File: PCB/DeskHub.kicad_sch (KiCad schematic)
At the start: 73 parts, among them J1 USB_A, J2 5V Barrel, U1 TUSB4041I, U3 Dual Voltage Regulator, Y1 ECS-240-20-30B-TR

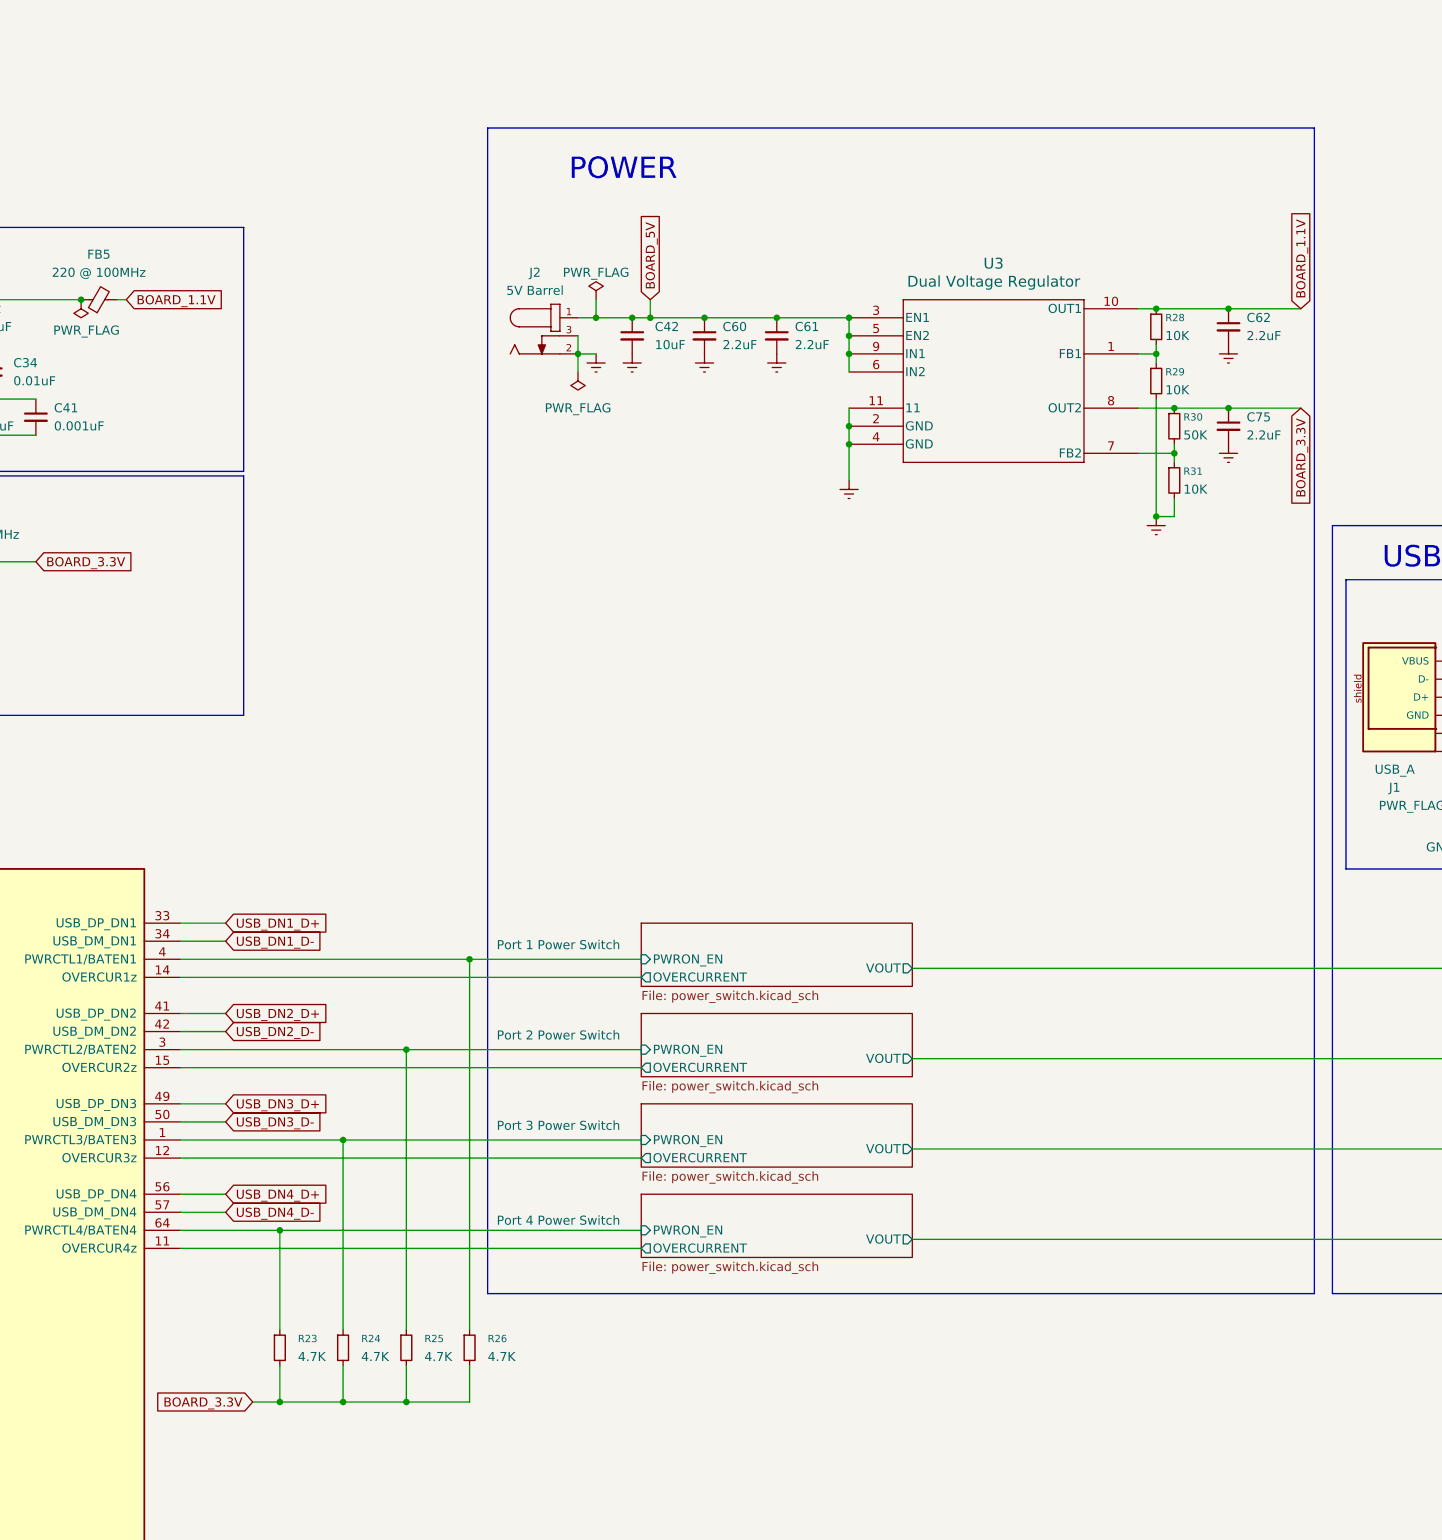
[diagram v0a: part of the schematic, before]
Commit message: add switching power supply
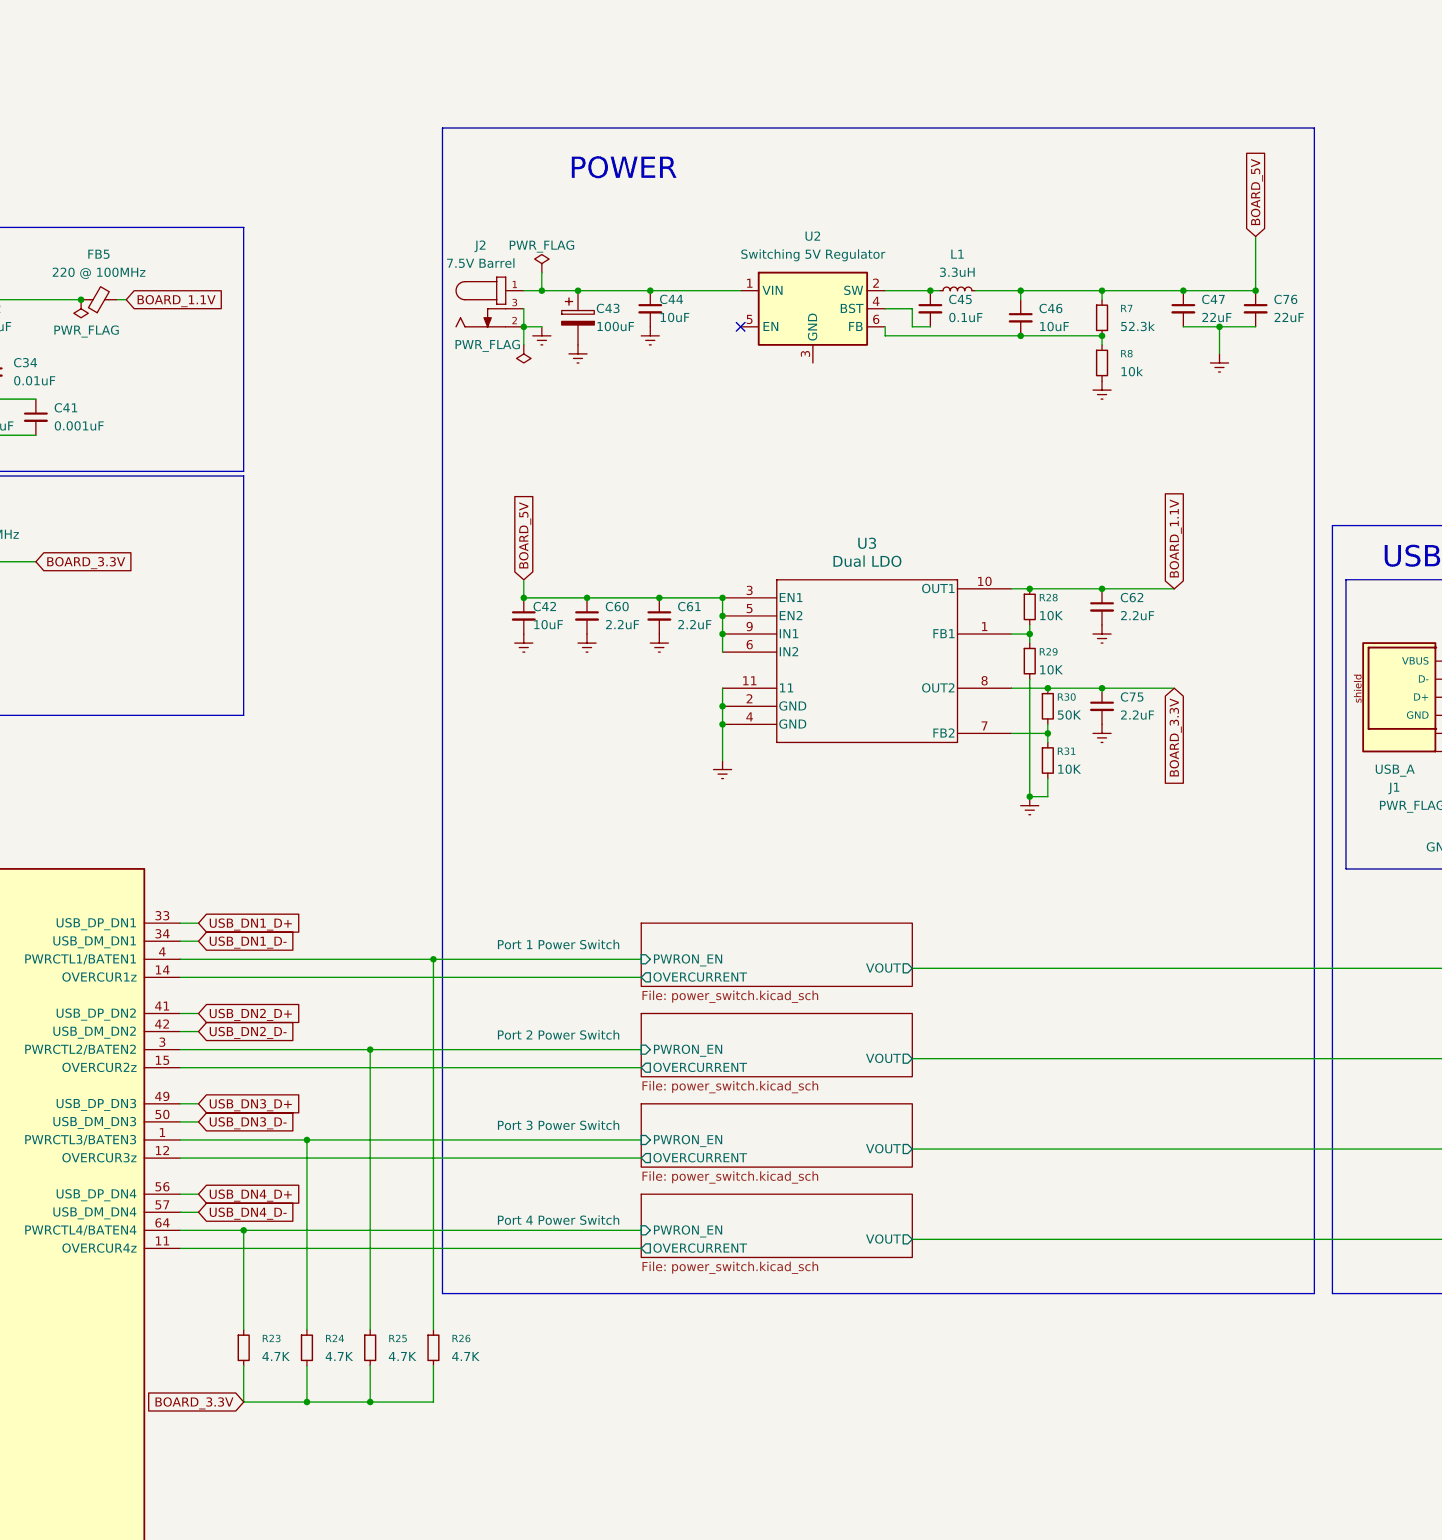
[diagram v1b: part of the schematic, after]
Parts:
- added C43: 100uF, symbol Device:C_Polarized
- added C44: 10uF, Capacitor_SMD:C_1206_3216Metric, symbol Device:C_Small
- added C45: 0.1uF, symbol Device:C_Small
- added C46: 10uF, symbol Device:C_Small
- added C47, C76: 22uF, symbol Device:C_Small
- added L1: 3.3uH, symbol Device:L_Small
- added R7: 52.3k, symbol Device:R_Small
- added R8: 10k, symbol Device:R_Small
- added U2: Switching 5V Regulator, Package_TO_SOT_SMD:SOT-563, symbol Regulator_Switching:AP62300Z6
- J2: value 5V Barrel -> 7.5V Barrel
- U3: value Dual Voltage Regulator -> Dual LDO
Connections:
- net BOARD_5V: now also C46.1, C47.1, C76.1, L1.2, R7.1; no longer J2.1
- net Earth: now also C43.2, C44.2, C47.2, C76.2, R8.2
- new net: C45.1, L1.1, U2.2 (SW)
- new net: C43.1, C44.1, J2.1, U2.1 (VIN)
- new net: C46.2, R7.2, R8.1, U2.6 (FB)
- new net: C45.2, U2.4 (BST)
- no-connect marks 5 -> 6
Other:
- moved on the sheet: C42, C60, C61, C62, C75, J2, R23, R24, R25, R26, R28, R29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

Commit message: work on pcb new power
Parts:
- removed C46: 10uF, symbol Device:C_Small
- C43: footprint (none) -> Capacitor_SMD:CP_Elec_6.3x7.7
- C45: footprint (none) -> Capacitor_SMD:C_0402_1005Metric
- C47, C76: footprint (none) -> Capacitor_SMD:C_0201_0603Metric
- L1: footprint (none) -> my_global:NRS5030T3R3MMGJ
- R28, R29, R30, R31, R7, R8: footprint (none) -> Resistor_SMD:R_0402_1005Metric
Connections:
- net Earth: now also U2.3 (GND)
- net VIN: now reaches C43.1, C44.1, J2.1, U2.1 (VIN)
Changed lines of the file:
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@@
 	)
 	(junction
+		(at 243.84 38.1)
+		(diameter 0)
+		(color 0 0 0 0)
+	)
+	(junction
 		(at 97.79 52.07)
 		(diameter 0)
@@
 	)
 	(junction
-		(at 289.56 44.45)
-		(diameter 0)
-		(color 0 0 0 0)
-	)
-	(junction
 		(at 119.38 76.2)
 		(diameter 0)
@@
 	)
 	(junction
-		(at 289.56 38.1)
-		(diameter 0)
-		(color 0 0 0 0)
-	)
-	(junction
 		(at 100.33 53.34)
 		(diameter 0)
@@
 	(wire
 		(pts
-			(xy 237.49 38.1) (xy 250.19 38.1)
+			(xy 237.49 38.1) (xy 243.84 38.1)
 		)
 		(stroke
@@
 	(wire
 		(pts
-			(xy 289.56 44.45) (xy 300.99 44.45)
-		)
-		(stroke
-			(width 0)
-			(type default)
-		)
-	)
-	(wire
-		(pts
 			(xy 383.54 113.03) (xy 383.54 114.3)
 		)
@@
 	(wire
 		(pts
-			(xy 289.56 44.45) (xy 270.51 44.45)
+			(xy 270.51 44.45) (xy 300.99 44.45)
 		)
 		(stroke
@@
 	(wire
 		(pts
+			(xy 243.84 34.29) (xy 243.84 38.1)
+		)
+		(stroke
+			(width 0)
+			(type default)
+		)
+	)
+	(wire
+		(pts
 			(xy 140.97 114.3) (xy 140.97 111.76)
 		)
@@
 	(wire
 		(pts
-			(xy 289.56 39.37) (xy 289.56 38.1)
-		)
-		(stroke
-			(width 0)
-			(type default)
-		)
-	)
-	(wire
-		(pts
 			(xy 85.09 39.37) (xy 95.25 39.37)
 		)
@@
 	(wire
 		(pts
-			(xy 289.56 38.1) (xy 300.99 38.1)
-		)
-		(stroke
-			(width 0)
-			(type default)
-		)
-	)
-	(wire
-		(pts
 			(xy 364.49 130.81) (xy 363.22 130.81)
 		)
@@
 	(wire
 		(pts
-			(xy 283.21 38.1) (xy 289.56 38.1)
+			(xy 283.21 38.1) (xy 300.99 38.1)
 		)
 		(stroke
@@
 	(wire
 		(pts
+			(xy 243.84 38.1) (xy 250.19 38.1)
+		)
+		(stroke
+			(width 0)
+			(type default)
+		)
+	)
+	(wire
+		(pts
 			(xy 113.03 53.34) (xy 125.73 53.34)
 		)
@@
 		)
 	)
+	(global_label "VIN"
+		(shape input)
+		(at 243.84 34.29 90)
+		(fields_autoplaced yes)
+		(effects
+			(font
+				(size 1.27 1.27)
+			)
+			(justify left)
+		)
+		(property "Intersheetrefs" "${INTERSHEET_REFS}"
+			(at 243.84 28.2809 90)
+			(effects
+				(font
+					(size 1.27 1.27)
+				)
+				(justify left)
+				(hide yes)
+			)
+		)
+	)
 	(global_label "USB_DN3_D-"
 		(shape input)
@@
 		(polyline
 			(pts
-				(xy 171.45 163.83) (xy 171.45 168.91) (xy 172.72 168.91) (xy 172.72 163.83)
+				(xy 171.45 138.43) (xy 171.45 143.51) (xy 172.72 143.51) (xy 172.72 138.43)
 			)
 			(stroke
@@
 		(polyline
 			(pts
-				(xy 171.45 138.43) (xy 171.45 143.51) (xy 172.72 143.51) (xy 172.72 138.43)
+				(xy 171.45 163.83) (xy 171.45 168.91) (xy 172.72 168.91) (xy 172.72 163.83)
 			)
 			(stroke
@@
 			)
 		)
-		(property "Footprint" ""
+		(property "Footprint" "my_global:NRS5030T3R3MMGJ"
 			(at 280.67 38.1 0)
 			(effects
@@
 			)
 		)
-		(property "Footprint" ""
+		(property "Footprint" "Capacitor_SMD:CP_Elec_6.3x7.7"
 			(at 228.2952 45.72 0)
 			(effects
@@
 	)
 	(symbol
-		(lib_id "Device:C_Small")
-		(at 289.56 41.91 0)
-		(unit 1)
-		(exclude_from_sim no)
-		(in_bom yes)
-		(on_board yes)
-		(dnp no)
-		(property "Reference" "C46"
-			(at 292.1 40.6462 0)
-			(effects
-				(font
-					(size 1.27 1.27)
-				)
-				(justify left)
-			)
-		)
-		(property "Value" "10uF"
-			(at 292.1 43.1862 0)
-			(effects
-				(font
-					(size 1.27 1.27)
-				)
-				(justify left)
-			)
-		)
-		(property "Footprint" ""
-			(at 289.56 41.91 0)
-			(effects
-				(font
-					(size 1.27 1.27)
-				)
-				(hide yes)
-			)
-		)
-		(property "Datasheet" "~"
-			(at 289.56 41.91 0)
-			(effects
-				(font
-					(size 1.27 1.27)
-				)
-				(hide yes)
-			)
-		)
-		(property "Description" "Unpolarized capacitor, small symbol"
-			(at 289.56 41.91 0)
-			(effects
-				(font
-					(size 1.27 1.27)
-				)
-				(hide yes)
-			)
-		)
-		(pin "1"
-		)
-		(pin "2"
-		)
-		(instances
-			(project "DeskHub"
-				(path "/d26b879a-ad2a-41ae-bbd0-9e3e439085d9"
-					(reference "C46")
-					(unit 1)
-				)
-			)
-		)
-	)
-	(symbol
 		(lib_id "power:Earth")
 		(at 87.63 220.98 0)
@@
 			)
 		)
-		(property "Footprint" ""
+		(property "Footprint" "Resistor_SMD:R_0402_1005Metric"
 			(at 293.37 96.52 0)
 			(effects
@@
 			)
 		)
-		(property "Footprint" ""
+		(property "Footprint" "Capacitor_SMD:C_0402_1005Metric"
 			(at 276.86 40.64 0)
 			(effects
@@
 			)
 		)
-		(property "Footprint" ""
+		(property "Footprint" "Resistor_SMD:R_0402_1005Metric"
 			(at 290.83 90.17 0)
 			(effects
@@
 			)
 		)
-		(property "Footprint" ""
+		(property "Footprint" "Resistor_SMD:R_0402_1005Metric"
 			(at 293.37 104.14 0)
 			(effects
@@
 			)
 		)
-		(property "Footprint" ""
+		(property "Footprint" "Resistor_SMD:R_0402_1005Metric"
 			(at 300.99 48.26 0)
 			(effects
@@
 	)
 	(symbol
+		(lib_id "power:Earth")
+		(at 260.35 48.26 0)
+		(unit 1)
+		(exclude_from_sim no)
+		(in_bom yes)
+		(on_board yes)
+		(dnp no)
+		(fields_autoplaced yes)
+		(property "Reference" "#PWR049"
+			(at 260.35 54.61 0)
+			(effects
+				(font
+					(size 1.27 1.27)
+				)
+				(hide yes)
+			)
+		)
+		(property "Value" "Earth"
+			(at 260.35 52.07 0)
+			(effects
+				(font
+					(size 1.27 1.27)
+				)
+				(hide yes)
+			)
+		)
+		(property "Footprint" ""
+			(at 260.35 48.26 0)
+			(effects
+				(font
+					(size 1.27 1.27)
+				)
+				(hide yes)
+			)
+		)
+		(property "Datasheet" "~"
+			(at 260.35 48.26 0)
+			(effects
+				(font
+					(size 1.27 1.27)
+				)
+				(hide yes)
+			)
+		)
+		(property "Description" ""
+			(at 260.35 48.26 0)
+			(effects
+				(font
+					(size 1.27 1.27)
+				)
+			)
+		)
+		(pin "1"
+		)
+		(instances
+			(project "DeskHub"
+				(path "/d26b879a-ad2a-41ae-bbd0-9e3e439085d9"
+					(reference "#PWR049")
+					(unit 1)
+				)
+			)
+		)
+	)
+	(symbol
 		(lib_id "ECS-240-20-30B-TR:ECS-240-20-30B-TR")
 		(at 53.34 171.45 0)
@@
 			)
 		)
-		(property "Footprint" ""
+		(property "Footprint" "Resistor_SMD:R_0402_1005Metric"
 			(at 290.83 82.55 0)
 			(effects
@@
 			)
 		)
-		(property "Footprint" ""
+		(property "Footprint" "Resistor_SMD:R_0402_1005Metric"
 			(at 300.99 41.91 0)
 			(effects
@@
 			)
 		)
-		(property "Footprint" ""
+		(property "Footprint" "Capacitor_SMD:C_0201_0603Metric"
 			(at 312.42 40.64 0)
 			(effects
@@
 			)
 		)
-		(property "Footprint" ""
+		(property "Footprint" "Capacitor_SMD:C_0201_0603Metric"
 			(at 322.58 40.64 0)
 			(effects
